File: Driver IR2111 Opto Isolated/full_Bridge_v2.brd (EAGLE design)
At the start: 20.6 x 58.7 mm, 20 parts

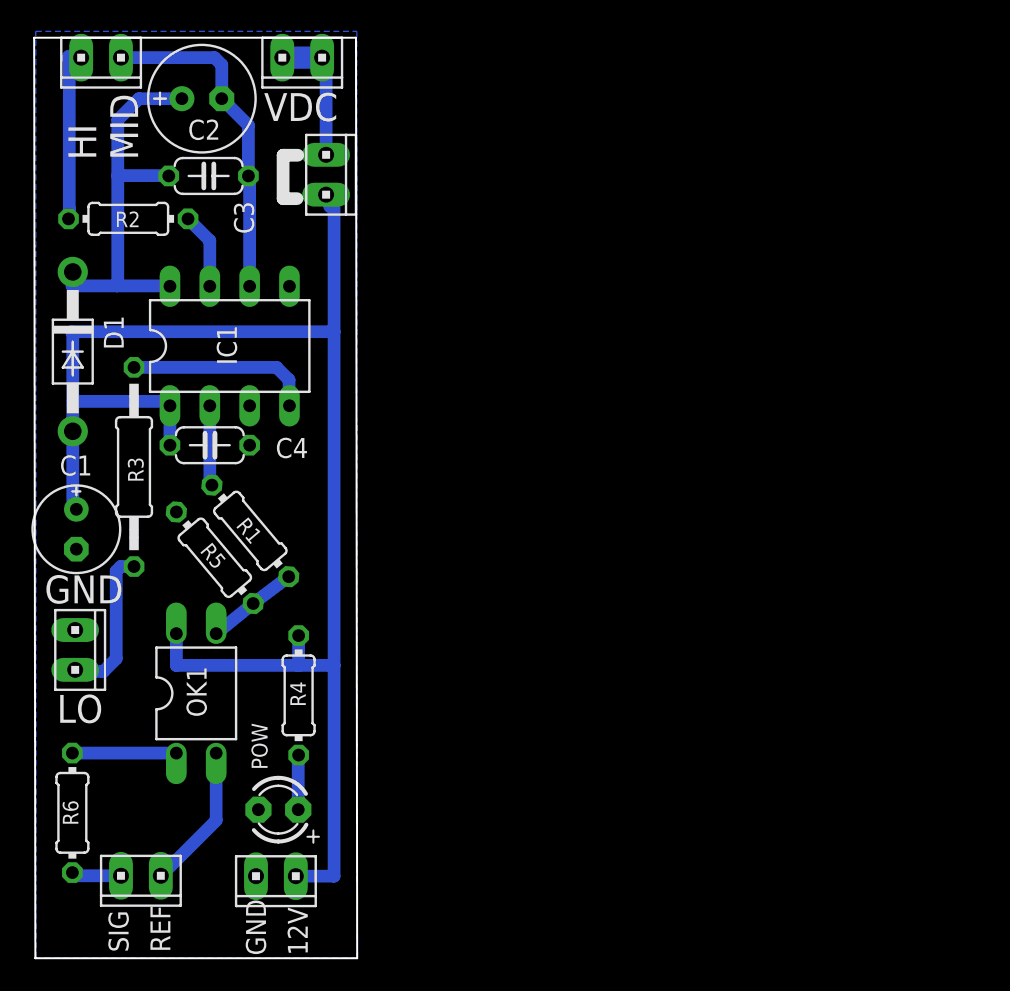
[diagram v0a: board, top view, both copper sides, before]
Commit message: IR2111 optical isolated driver updated
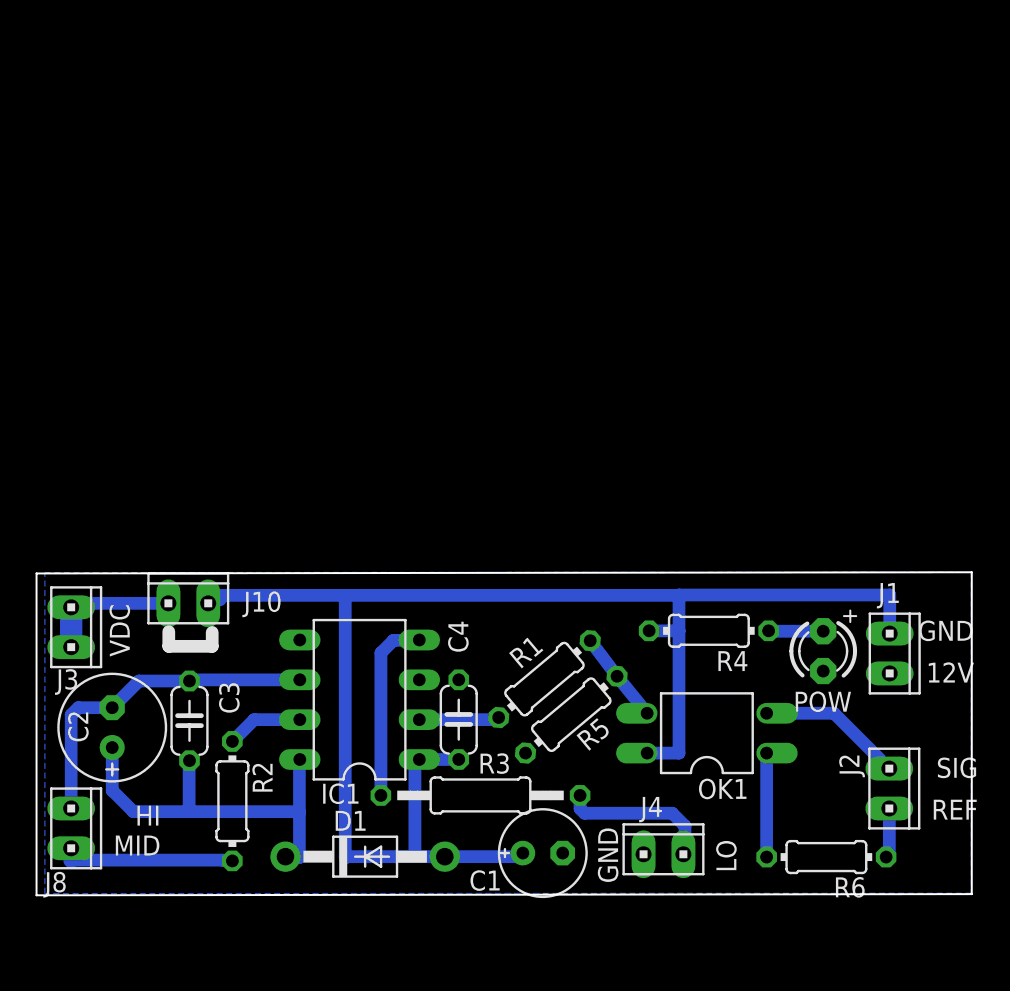
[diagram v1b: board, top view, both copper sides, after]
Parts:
- C1, C2: value (none) -> 100uF
- C3, C4: value (none) -> 100nF
- D1: value 1N4004 -> FR107
- R1, R2, R3, R6: value (none) -> 100R
- R4, R5: value (none) -> 1k
- moved J8 49.2 mm to (2.29, 4.32), turned to 270 degrees
- moved R6 48.2 mm to (50.4, 2.49), turned to 180 degrees
- moved J2 48.0 mm to (54.5, 6.86), turned to 270 degrees
- moved J1 41.6 mm to (54.5, 15.5), turned to 270 degrees
- moved C2 40.5 mm to (4.90, 10.7), turned to 90 degrees
- moved J4 39.7 mm to (40.1, 2.67), turned to 0 degrees
- moved J3 39.2 mm to (2.29, 17.1), turned to 270 degrees
- moved R2 37.7 mm to (12.6, 6.05), turned to 270 degrees
- moved D1 37.2 mm to (21.0, 2.51), turned to 0 degrees
- moved C1 36.2 mm to (32.4, 2.74), turned to 0 degrees
- moved POW 36.2 mm to (50.2, 15.6), turned to 270 degrees
- moved C3 34.8 mm to (9.83, 11.2), turned to 90 degrees
- moved OK1 32.7 mm to (42.8, 10.4), turned to 90 degrees
- moved R3 30.4 mm to (28.4, 6.42), turned to 0 degrees
- moved J10 28.7 mm to (9.75, 18.7), turned to 0 degrees
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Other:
- board size 20.6 x 58.7 mm -> 59.6 x 20.6 mm
